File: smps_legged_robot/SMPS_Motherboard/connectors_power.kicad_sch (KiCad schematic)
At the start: 1 part, among them J7 PJ-082BH

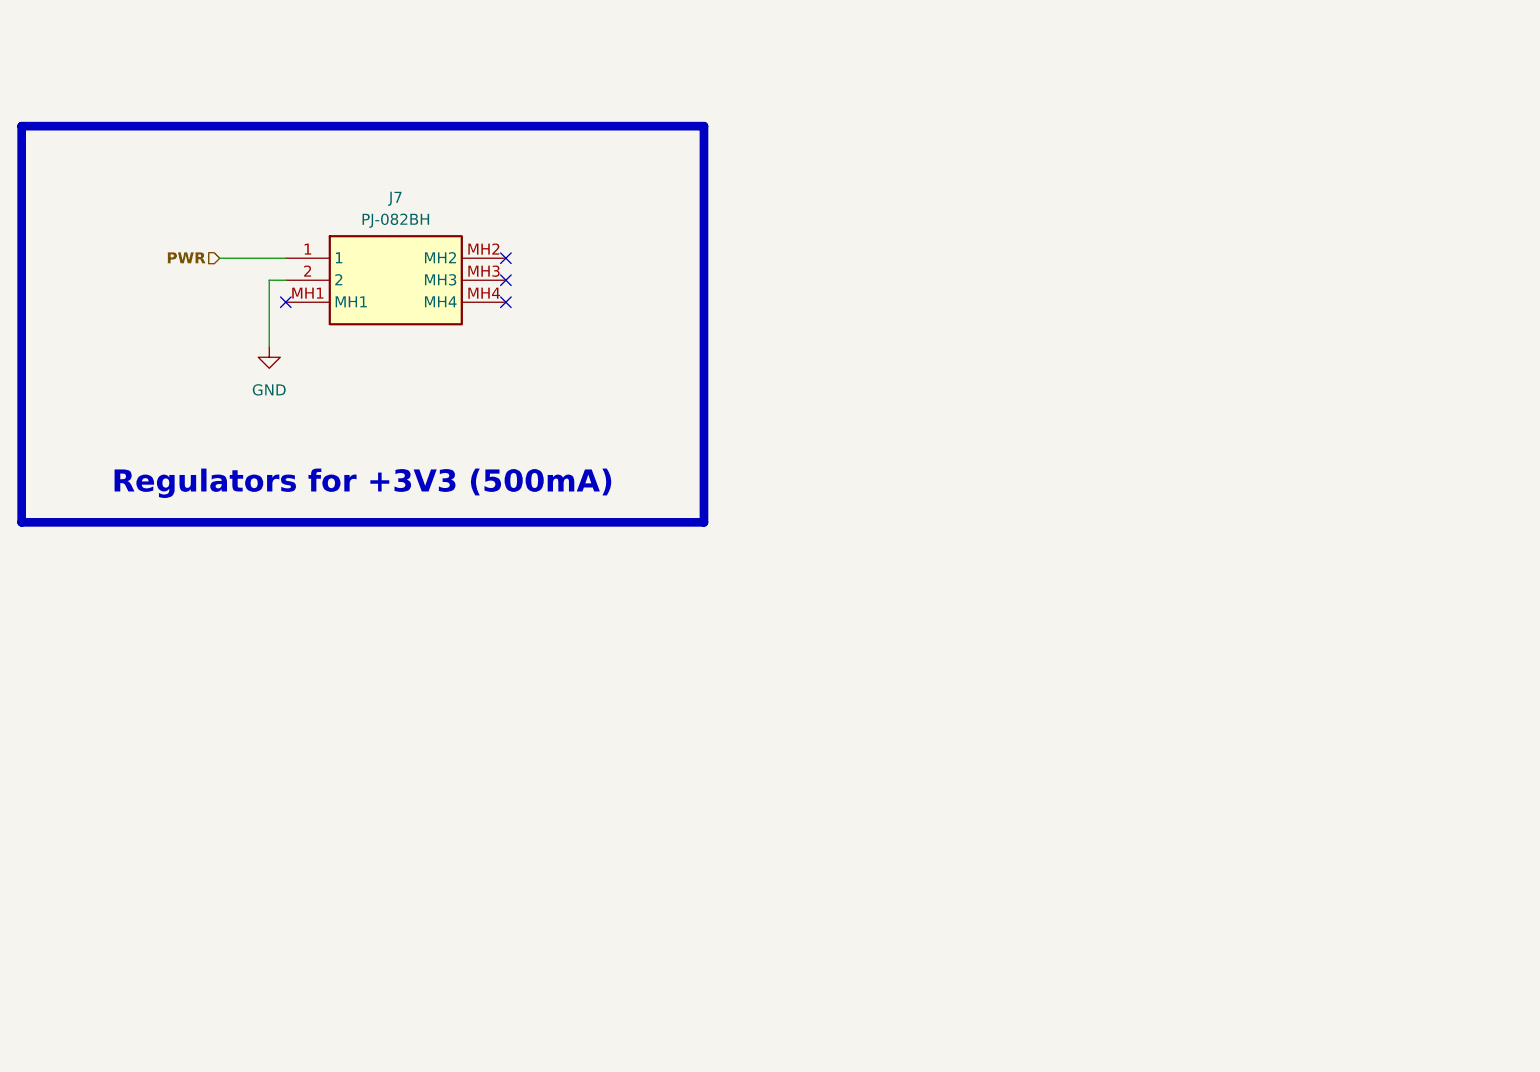
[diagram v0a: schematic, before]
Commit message: Buck module finished pending review
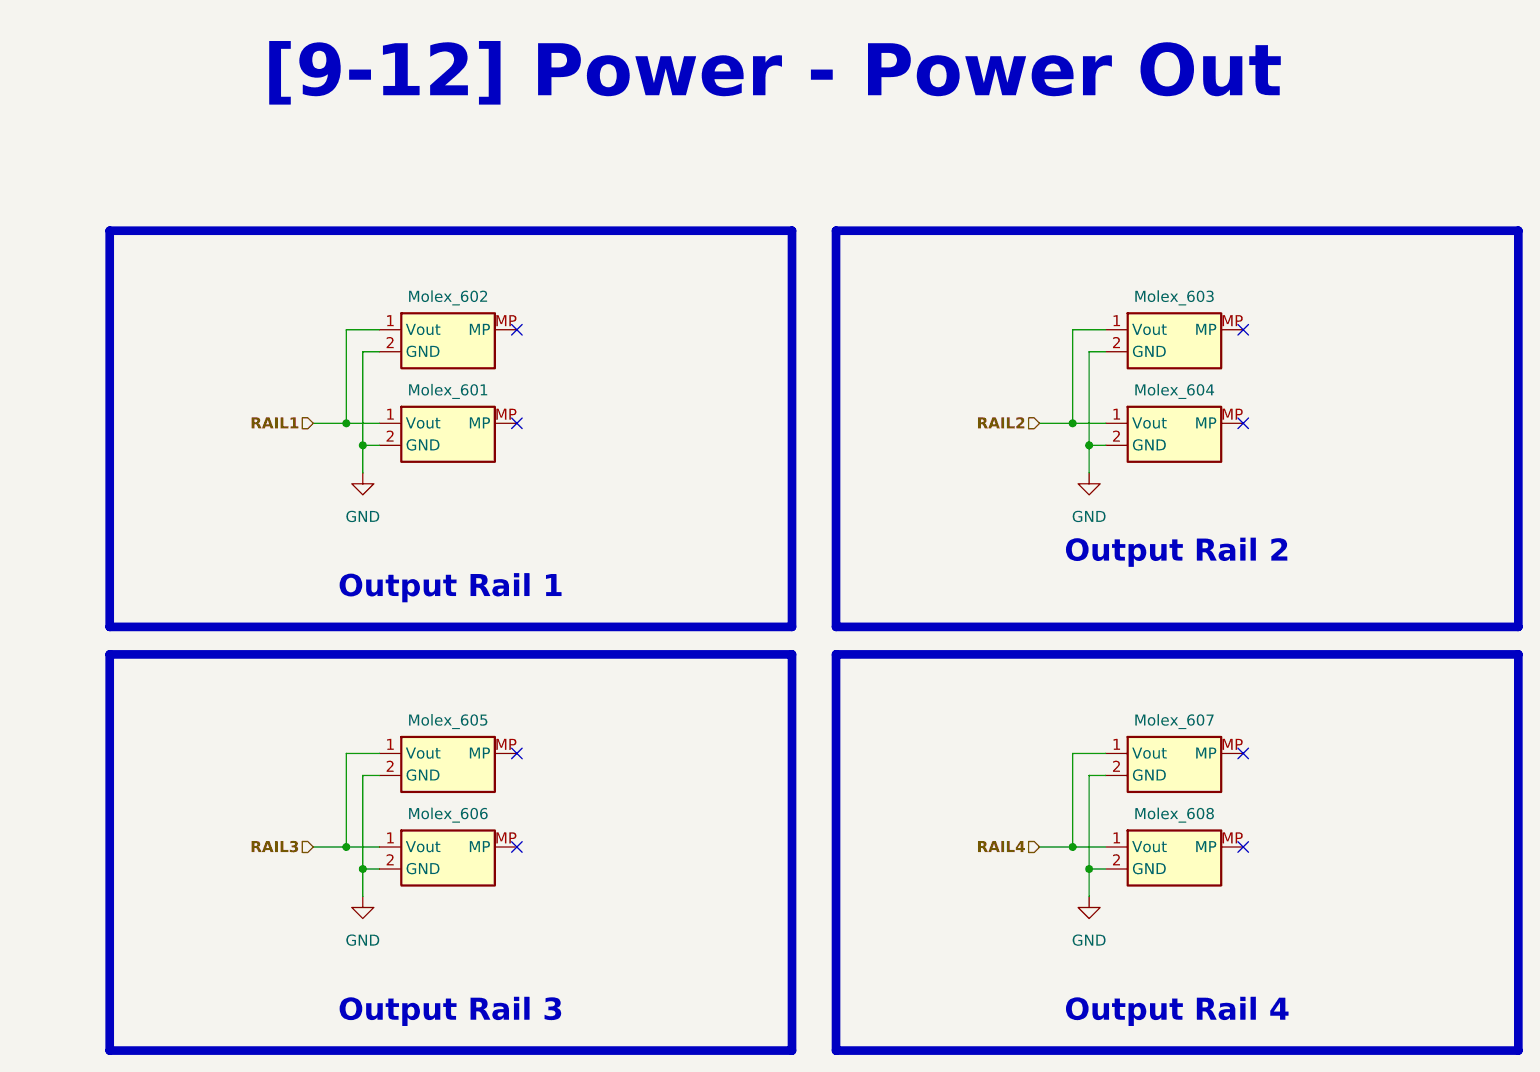
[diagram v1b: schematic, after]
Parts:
- removed J7: PJ-082BH, PJ082BH, symbol PJ-082BH:PJ-082BH
- added Molex_601, Molex_602, Molex_603, Molex_604, Molex_605, Molex_606, Molex_607, Molex_608: ~, 0_connectors:172448-YY02, symbol 0_connectors:Molex__755611500
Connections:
- net GND: now also Molex_601.2 (GND), Molex_602.2 (GND), Molex_603.2 (GND), Molex_604.2 (GND), Molex_605.2 (GND), Molex_606.2 (GND), Molex_607.2 (GND), Molex_608.2 (GND)
- new net RAIL1: Molex_601.1 (Vout), Molex_602.1 (Vout)
- new net RAIL2: Molex_603.1 (Vout), Molex_604.1 (Vout)
- new net RAIL3: Molex_605.1 (Vout), Molex_606.1 (Vout)
- new net RAIL4: Molex_607.1 (Vout), Molex_608.1 (Vout)
- no-connect marks 4 -> 8
